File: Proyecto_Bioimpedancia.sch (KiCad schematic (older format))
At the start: 69 parts, among them J1 Jumper, J2 Jumper, J3 Jumper_Calibration, J4 Jumper, J5 Jumper, J6 Jumper, P1 SD_LAPIZ, P10 RS-232, P11 SOURCE_2, P12 RESET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

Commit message: PCB version final
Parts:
- removed P10: RS-232, Socket_Strips:Socket_Strip_Straight_1x03_Pitch2.54mm, symbol CONN_01X03
- removed P6: I2C_1, Socket_Strips:Socket_Strip_Straight_1x02_Pitch2.54mm, symbol CONN_01X02
- removed P7: I2C_2, Socket_Strips:Socket_Strip_Straight_1x02_Pitch2.54mm, symbol CONN_01X02
- added C14: 0,1uF, Capacitors_SMD:C_0805_HandSoldering, symbol 0,1uF
- added P10: UNIVERSAL_PINS, Huellas:Universal_Path_80_Pins, symbol CONN_01X01
- added P6: I2C, Socket_Strips:Socket_Strip_Straight_2x04_Pitch2.54mm, symbol CONN_02X04
- added P7: CONN_01X04, Socket_Strips:Socket_Strip_Straight_1x04_Pitch2.54mm, symbol CONN_01X04
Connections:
- net AGND: now also P7.1 (P1)
- net RESET: now also C14.2
- net RXD: now also P7.3 (P3)
- net SCL_R: now also P6.1 (P1), P6.3 (P3), P6.5 (P5), P6.7 (P7)
- net SDA_R: now also P6.2 (P2), P6.4 (P4), P6.6 (P6), P6.8 (P8)
- net TXD: now also P7.2 (P2)
- new net: C14.1, P7.4 (P4)
- no-connect marks 0 -> 1
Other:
- note added: "Regleta Universal"
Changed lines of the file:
@@
 Text Label 5650 7310 0    39   ~ 0
 RESET
-$Comp
-L CONN_01X03 P10
-U 1 1 59AB4756
-P 5110 4440
-F 0 "P10" H 5110 4640 50  0000 C CNN
-F 1 "RS-232" V 5210 4440 50  0000 C CNN
-F 2 "Socket_Strips:Socket_Strip_Straight_1x03_Pitch2.54mm" H 5110 4440 50  0001 C CNN
-F 3 "" H 5110 4440 50  0000 C CNN
-	1    5110 4440
-	1    0    0    -1
-$EndComp
 Text Label 8220 1960 0    39   ~ 0
 REG2_6
-Text Label 4690 4440 0    39   ~ 0
+Text Label 5060 4400 0    39   ~ 0
 TXD
-Text Label 4690 4540 0    39   ~ 0
+Text Label 5060 4500 0    39   ~ 0
 RXD
-Text Label 4690 4340 0    39   ~ 0
+Text Label 5060 4300 0    39   ~ 0
 GND
 $Comp
@@
 Text Notes 4370 5780 0    59   ~ 0
 Pines Extras de Alimentacion\n
-$Comp
-L CONN_01X02 P6
-U 1 1 59B39B02
-P 3500 5530
-F 0 "P6" H 3500 5680 50  0000 C CNN
-F 1 "I2C_1" V 3600 5530 50  0000 C CNN
-F 2 "Socket_Strips:Socket_Strip_Straight_1x02_Pitch2.54mm" H 3500 5530 50  0001 C CNN
-F 3 "" H 3500 5530 50  0000 C CNN
-	1    3500 5530
-	1    0    0    -1
-$EndComp
-$Comp
-L CONN_01X02 P7
-U 1 1 59B39CA1
-P 3510 6040
-F 0 "P7" H 3510 6190 50  0000 C CNN
-F 1 "I2C_2" V 3610 6040 50  0000 C CNN
-F 2 "Socket_Strips:Socket_Strip_Straight_1x02_Pitch2.54mm" H 3510 6040 50  0001 C CNN
-F 3 "" H 3510 6040 50  0000 C CNN
-	1    3510 6040
-	1    0    0    -1
-$EndComp
-Text Label 3000 5480 0    39   ~ 0
+Text Label 3630 5800 2    39   ~ 0
 SDA_R
-Text Label 3000 5580 0    39   ~ 0
+Text Label 2530 5800 0    39   ~ 0
 SCL_R
-Text Label 3010 5990 0    39   ~ 0
+Text Label 3630 5700 2    39   ~ 0
 SDA_R
-Text Label 3010 6090 0    39   ~ 0
+Text Label 2530 5700 0    39   ~ 0
 SCL_R
 $Comp
@@
 	7920 1960 8220 1960
 Wire Wire Line
-	4910 4440 4690 4440
-Wire Wire Line
-	4910 4540 4690 4540
-Wire Wire Line
-	4690 4340 4910 4340
+	5280 4400 5060 4400
+Wire Wire Line
+	5280 4500 5060 4500
+Wire Wire Line
+	5060 4300 5280 4300
 Wire Wire Line
 	2810 7340 2560 7340
@@
 	5960 5640 4050 5640
 Wire Wire Line
-	3300 5480 3000 5480
-Wire Wire Line
-	3300 5580 3000 5580
-Wire Wire Line
-	3310 5990 3010 5990
-Wire Wire Line
-	3310 6090 3010 6090
+	3330 5800 3630 5800
+Wire Wire Line
+	2830 5800 2530 5800
+Wire Wire Line
+	3330 5700 3630 5700
+Wire Wire Line
+	2830 5700 2530 5700
 Wire Wire Line
 	5140 5990 5390 5990
@@
 	1    0    0    -1
 $EndComp
+$Comp
+L CONN_02X04 P6
+U 1 1 59D2F22B
+P 3080 5850
+F 0 "P6" H 3080 6100 50  0000 C CNN
+F 1 "I2C" H 3080 5600 50  0000 C CNN
+F 2 "Socket_Strips:Socket_Strip_Straight_2x04_Pitch2.54mm" H 3080 4650 50  0001 C CNN
+F 3 "" H 3080 4650 50  0000 C CNN
+	1    3080 5850
+	1    0    0    -1
+$EndComp
+Text Label 3630 6000 2    39   ~ 0
+SDA_R
+Text Label 3630 5900 2    39   ~ 0
+SDA_R
+Wire Wire Line
+	3330 6000 3630 6000
+Wire Wire Line
+	3330 5900 3630 5900
+Text Label 2530 6000 0    39   ~ 0
+SCL_R
+Text Label 2530 5900 0    39   ~ 0
+SCL_R
+Wire Wire Line
+	2830 6000 2530 6000
+Wire Wire Line
+	2830 5900 2530 5900
+$Comp
+L CONN_01X04 P7
+U 1 1 59D31E55
+P 5480 4450
+F 0 "P7" H 5480 4700 50  0000 C CNN
+F 1 "CONN_01X04" V 5580 4450 50  0000 C CNN
+F 2 "Socket_Strips:Socket_Strip_Straight_1x04_Pitch2.54mm" H 5480 4450 50  0001 C CNN
+F 3 "" H 5480 4450 50  0000 C CNN
+	1    5480 4450
+	1    0    0    -1
+$EndComp
+Wire Wire Line
+	5280 4600 5060 4600
+$Comp
+L 0,1uF C14
+U 1 1 59D32E4B
+P 4960 4600
+F 0 "C14" V 4910 4670 50  0000 L CNN
+F 1 "0,1uF" V 4900 4360 50  0000 L CNN
+F 2 "Capacitors_SMD:C_0805_HandSoldering" H 4870 4570 50  0001 C CNN
+F 3 "" H 4960 4600 50  0000 C CNN
+F 4 "478-1395-2-ND" H 5070 4770 118 0001 C CNN "CAP CER 0.1UF 50V X7R 0805"
+	1    4960 4600
+	0    1    1    0
+$EndComp
+Wire Wire Line
+	4860 4600 4410 4600
+Text Label 4410 4600 0    39   ~ 0
+RESET
+Wire Notes Line
+	6100 5730 6100 6410
+Wire Notes Line
+	6100 6410 6940 6410
+Wire Notes Line
+	6940 6410 6940 5730
+Wire Notes Line
+	6940 5730 6100 5730
+$Comp
+L CONN_01X01 P10
+U 1 1 59D34918
+P 6650 6090
+F 0 "P10" H 6650 6190 50  0000 C CNN
+F 1 "UNIVERSAL_PINS" V 6790 6090 50  0000 C CNN
+F 2 "Huellas:Universal_Path_80_Pins" H 6650 6090 50  0001 C CNN
+F 3 "" H 6650 6090 50  0000 C CNN
+	1    6650 6090
+	1    0    0    -1
+$EndComp
+NoConn ~ 6450 6090
+Text Notes 6180 5850 0    39   ~ 0
+Regleta Universal
 $EndSCHEMATC

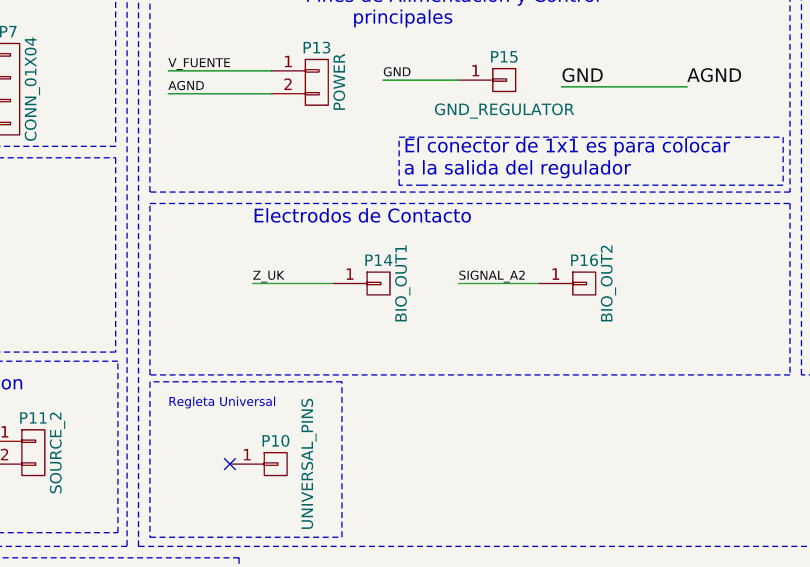
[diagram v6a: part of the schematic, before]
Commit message: Regleta Universal Añadida
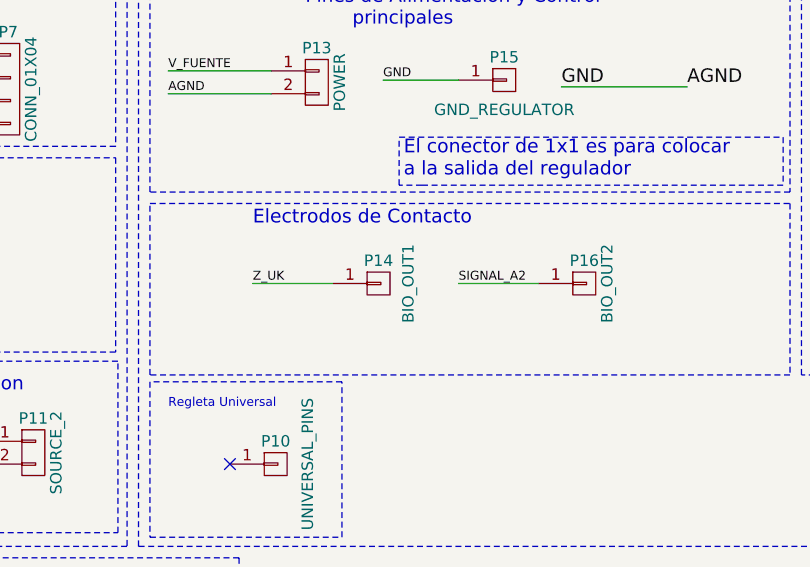
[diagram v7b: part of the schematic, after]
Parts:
- P10: footprint Huellas:Universal_Path_80_Pins -> Huellas:Universal_Path_300_Pins
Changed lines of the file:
@@
 P 7100 5300
 F 0 "P14" H 7100 5400 50  0000 C CNN
-F 1 "BIO_OUT1" V 7200 5300 50  0000 C CNN
+F 1 "BIO_OUT1" V 7230 5300 50  0000 C CNN
 F 2 "Connectors:SMA_THT_Jack_Straight" H 7100 5300 50  0001 C CNN
 F 3 "" H 7100 5300 50  0000 C CNN
@@
 F 0 "P10" H 6650 6190 50  0000 C CNN
 F 1 "UNIVERSAL_PINS" V 6790 6090 50  0000 C CNN
-F 2 "Huellas:Universal_Path_80_Pins" H 6650 6090 50  0001 C CNN
+F 2 "Huellas:Universal_Path_300_Pins" H 6650 6090 50  0001 C CNN
 F 3 "" H 6650 6090 50  0000 C CNN
 	1    6650 6090

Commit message: Version para placa
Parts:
- added P17: TOR_1, Mounting_Holes:MountingHole_3.2mm_M3_Pad_Via, symbol CONN_01X01
- added P18: TOR_2, Mounting_Holes:MountingHole_3.2mm_M3_Pad_Via, symbol CONN_01X01
- added P19: TOR_3, Mounting_Holes:MountingHole_3.2mm_M3_Pad_Via, symbol CONN_01X01
- added P20: TOR_4, Mounting_Holes:MountingHole_3.2mm_M3_Pad_Via, symbol CONN_01X01
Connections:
- no-connect marks 1 -> 5
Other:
- note added: "Tornillos para la PCB"
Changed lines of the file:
@@
 Text Notes 6180 5850 0    39   ~ 0
 Regleta Universal
+Wire Notes Line
+	7000 5730 7000 6410
+Wire Notes Line
+	7000 6410 8170 6410
+Wire Notes Line
+	7000 5730 9050 5730
+$Comp
+L CONN_01X01 P17
+U 1 1 59D7D59E
+P 7510 6070
+F 0 "P17" H 7510 6170 50  0000 C CNN
+F 1 "TOR_1" V 7610 6070 50  0000 C CNN
+F 2 "Mounting_Holes:MountingHole_3.2mm_M3_Pad_Via" H 7510 6070 50  0001 C CNN
+F 3 "" H 7510 6070 50  0000 C CNN
+	1    7510 6070
+	1    0    0    -1
+$EndComp
+$Comp
+L CONN_01X01 P18
+U 1 1 59D7DB22
+P 7920 6070
+F 0 "P18" H 7920 6170 50  0000 C CNN
+F 1 "TOR_2" V 8020 6070 50  0000 C CNN
+F 2 "Mounting_Holes:MountingHole_3.2mm_M3_Pad_Via" H 7920 6070 50  0001 C CNN
+F 3 "" H 7920 6070 50  0000 C CNN
+	1    7920 6070
+	1    0    0    -1
+$EndComp
+$Comp
+L CONN_01X01 P19
+U 1 1 59D7E0E8
+P 8320 6070
+F 0 "P19" H 8320 6170 50  0000 C CNN
+F 1 "TOR_3" V 8420 6070 50  0000 C CNN
+F 2 "Mounting_Holes:MountingHole_3.2mm_M3_Pad_Via" H 8320 6070 50  0001 C CNN
+F 3 "" H 8320 6070 50  0000 C CNN
+	1    8320 6070
+	1    0    0    -1
+$EndComp
+$Comp
+L CONN_01X01 P20
+U 1 1 59D7E0EE
+P 8730 6070
+F 0 "P20" H 8730 6170 50  0000 C CNN
+F 1 "TOR_4" V 8830 6070 50  0000 C CNN
+F 2 "Mounting_Holes:MountingHole_3.2mm_M3_Pad_Via" H 8730 6070 50  0001 C CNN
+F 3 "" H 8730 6070 50  0000 C CNN
+	1    8730 6070
+	1    0    0    -1
+$EndComp
+Wire Notes Line
+	8160 6410 9050 6410
+Wire Notes Line
+	9050 6410 9050 5730
+Text Notes 7730 5830 0    39   ~ 0
+Tornillos para la PCB
+NoConn ~ 8530 6070
+NoConn ~ 8120 6070
+NoConn ~ 7720 6070
+NoConn ~ 7310 6070
 $EndSCHEMATC
